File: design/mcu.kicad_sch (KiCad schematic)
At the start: 30 parts, among them J2 SWD_01X04, J3 DEBUG_SPI, U6 STM32H750VBTx, X1 ASTX-H11-25.000MHZ-T

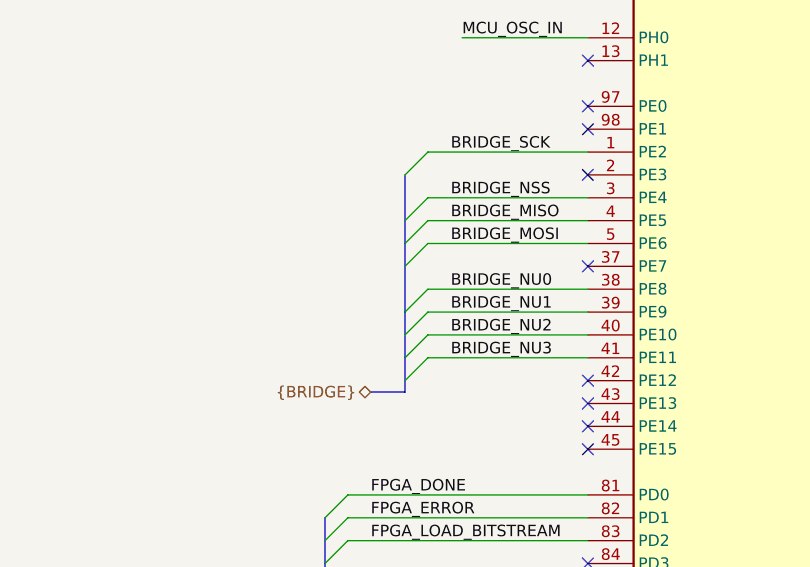
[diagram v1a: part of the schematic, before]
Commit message: Added RAM layout
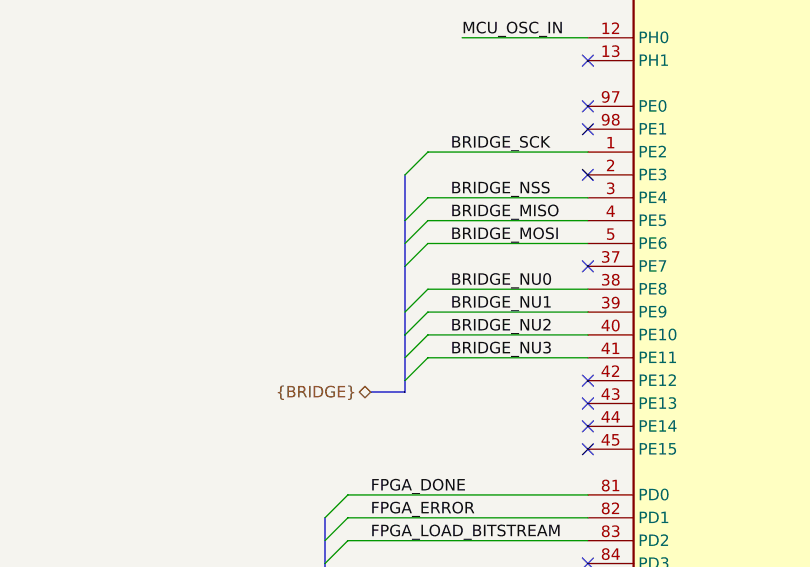
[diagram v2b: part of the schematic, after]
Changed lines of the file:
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@@
   (junction (at 236.22 25.4))
   (junction (at 262.89 26.67))
-  (no_connect (at 168.91 134.62))
-  (no_connect (at 168.91 86.36))
+  (no_connect (at 168.91 106.68))
+  (no_connect (at 168.91 127))
+  (no_connect (at 168.91 60.96))
+  (no_connect (at 168.91 129.54))
+  (no_connect (at 168.91 149.86))
   (no_connect (at 123.19 109.22))
   (no_connect (at 168.91 121.92))
+  (no_connect (at 168.91 53.34))
+  (no_connect (at 168.91 104.14))
+  (no_connect (at 123.19 144.78))
+  (no_connect (at 123.19 129.54))
+  (no_connect (at 168.91 116.84))
+  (no_connect (at 168.91 154.94))
+  (no_connect (at 168.91 119.38))
+  (no_connect (at 123.19 124.46))
+  (no_connect (at 168.91 50.8))
+  (no_connect (at 123.19 147.32))
+  (no_connect (at 168.91 86.36))
+  (no_connect (at 168.91 109.22))
+  (no_connect (at 123.19 162.56))
+  (no_connect (at 123.19 121.92))
+  (no_connect (at 168.91 170.18))
+  (no_connect (at 168.91 147.32))
+  (no_connect (at 168.91 167.64))
+  (no_connect (at 123.19 149.86))
+  (no_connect (at 123.19 142.24))
+  (no_connect (at 123.19 154.94))
+  (no_connect (at 168.91 142.24))
+  (no_connect (at 168.91 139.7))
+  (no_connect (at 168.91 134.62))
+  (no_connect (at 168.91 172.72))
+  (no_connect (at 168.91 165.1))
+  (no_connect (at 168.91 101.6))
+  (no_connect (at 123.19 91.44))
+  (no_connect (at 168.91 160.02))
+  (no_connect (at 168.91 68.58))
+  (no_connect (at 123.19 127))
+  (no_connect (at 168.91 162.56))
+  (no_connect (at 168.91 124.46))
+  (no_connect (at 168.91 63.5))
+  (no_connect (at 123.19 152.4))
+  (no_connect (at 168.91 114.3))
+  (no_connect (at 168.91 152.4))
   (no_connect (at 168.91 111.76))
-  (no_connect (at 168.91 172.72))
-  (no_connect (at 168.91 152.4))
+  (no_connect (at 123.19 86.36))
+  (no_connect (at 123.19 99.06))
+  (no_connect (at 168.91 137.16))
+  (no_connect (at 168.91 144.78))
+  (no_connect (at 123.19 93.98))
+  (no_connect (at 168.91 55.88))
   (no_connect (at 123.19 160.02))
-  (no_connect (at 168.91 154.94))
-  (no_connect (at 168.91 144.78))
-  (no_connect (at 123.19 142.24))
-  (no_connect (at 168.91 165.1))
-  (no_connect (at 168.91 119.38))
-  (no_connect (at 168.91 124.46))
-  (no_connect (at 123.19 91.44))
   (no_connect (at 168.91 66.04))
-  (no_connect (at 123.19 144.78))
-  (no_connect (at 168.91 167.64))
-  (no_connect (at 123.19 127))
   (no_connect (at 123.19 157.48))
-  (no_connect (at 168.91 127))
+  (no_connect (at 168.91 58.42))
   (no_connect (at 168.91 48.26))
-  (no_connect (at 123.19 152.4))
-  (no_connect (at 168.91 170.18))
-  (no_connect (at 123.19 162.56))
-  (no_connect (at 168.91 142.24))
-  (no_connect (at 168.91 63.5))
-  (no_connect (at 168.91 147.32))
-  (no_connect (at 123.19 99.06))
-  (no_connect (at 168.91 58.42))
-  (no_connect (at 123.19 124.46))
-  (no_connect (at 168.91 139.7))
-  (no_connect (at 168.91 50.8))
-  (no_connect (at 168.91 106.68))
-  (no_connect (at 123.19 86.36))
-  (no_connect (at 168.91 116.84))
-  (no_connect (at 168.91 109.22))
-  (no_connect (at 168.91 101.6))
-  (no_connect (at 168.91 60.96))
-  (no_connect (at 123.19 154.94))
-  (no_connect (at 123.19 129.54))
-  (no_connect (at 123.19 147.32))
-  (no_connect (at 123.19 93.98))
-  (no_connect (at 168.91 104.14))
-  (no_connect (at 168.91 149.86))
-  (no_connect (at 168.91 53.34))
-  (no_connect (at 168.91 114.3))
-  (no_connect (at 168.91 129.54))
-  (no_connect (at 168.91 55.88))
-  (no_connect (at 168.91 162.56))
-  (no_connect (at 168.91 137.16))
-  (no_connect (at 168.91 160.02))
-  (no_connect (at 123.19 121.92))
-  (no_connect (at 168.91 68.58))
-  (no_connect (at 123.19 149.86))
   (bus_entry (at 93.98 137.16) (size 2.54 -2.54))
   (bus_entry (at 93.98 139.7) (size 2.54 -2.54))
@@
   (bus (pts (xy 93.98 142.24) (xy 93.98 143.51)))
   (bus (pts (xy 99.06 123.19) (xy 102.87 123.19)))
-  (bus (pts (xy 102.87 99.06) (xy 102.87 106.68)))
-  (bus (pts (xy 102.87 106.68) (xy 102.87 114.3)))
-  (bus (pts (xy 102.87 114.3) (xy 102.87 119.38)))
-  (bus (pts (xy 102.87 119.38) (xy 102.87 123.19)))
+  (bus (pts (xy 102.87 99.06) (xy 102.87 104.14)))
+  (bus (pts (xy 102.87 104.14) (xy 102.87 109.22)))
+  (bus (pts (xy 102.87 109.22) (xy 102.87 116.84)))
+  (bus (pts (xy 102.87 116.84) (xy 102.87 121.92)))
+  (bus (pts (xy 102.87 121.92) (xy 102.87 123.19)))
   (bus (pts (xy 187.96 73.66) (xy 187.96 76.2)))
   (bus (pts (xy 187.96 76.2) (xy 187.96 81.28)))

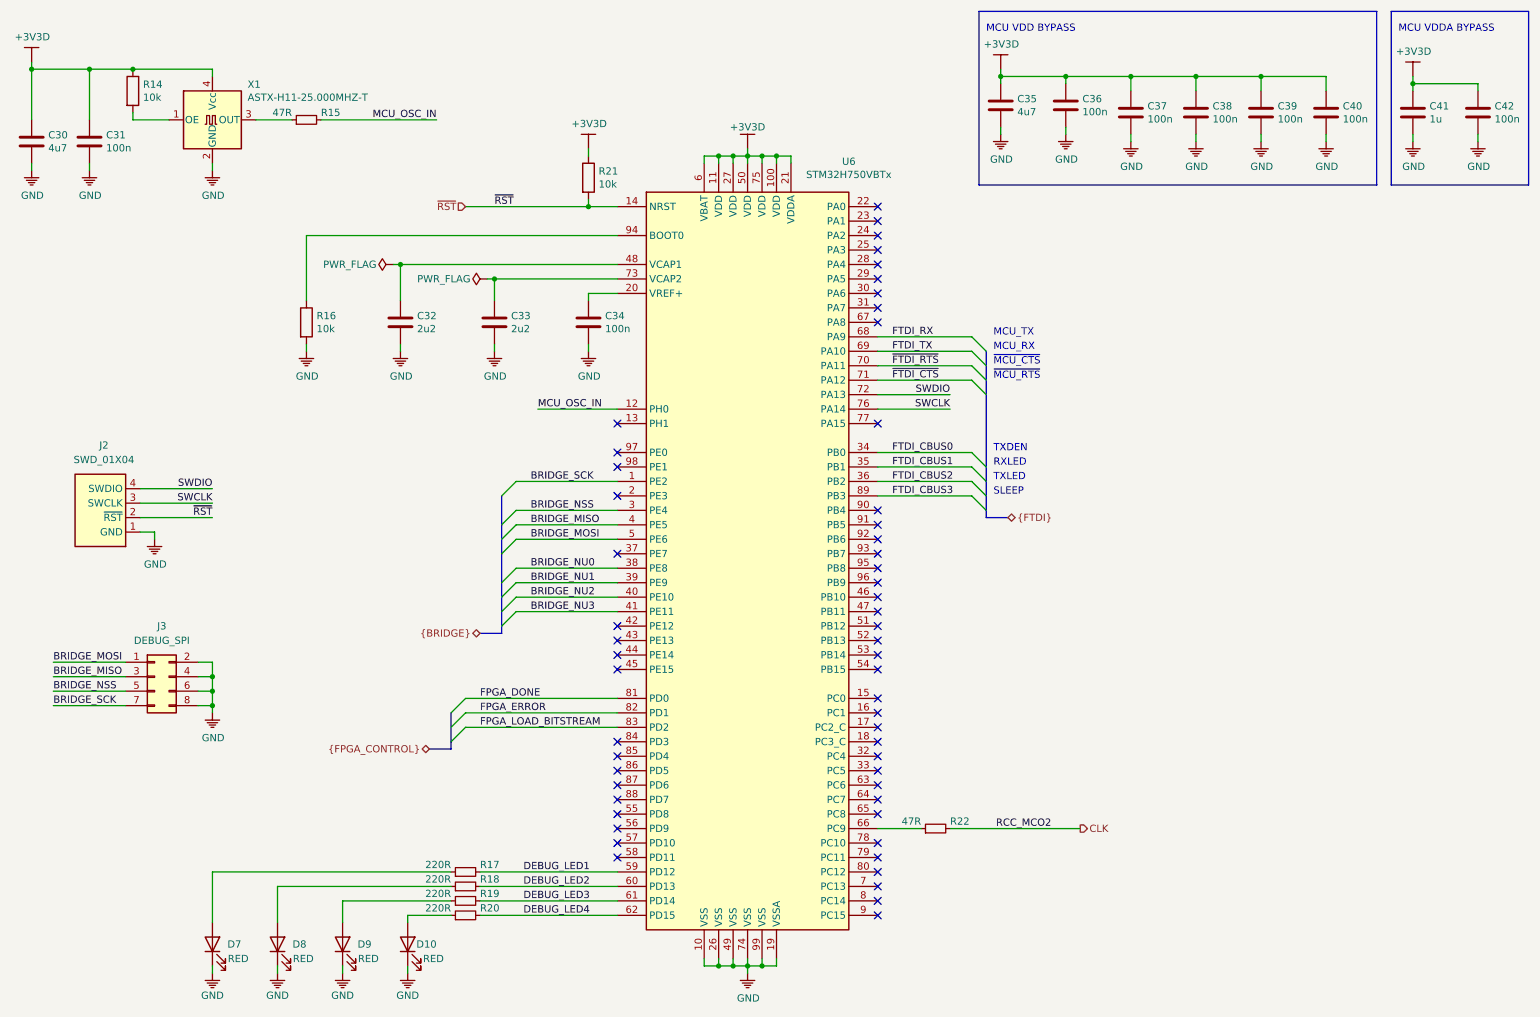
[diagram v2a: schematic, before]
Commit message: Updated layout
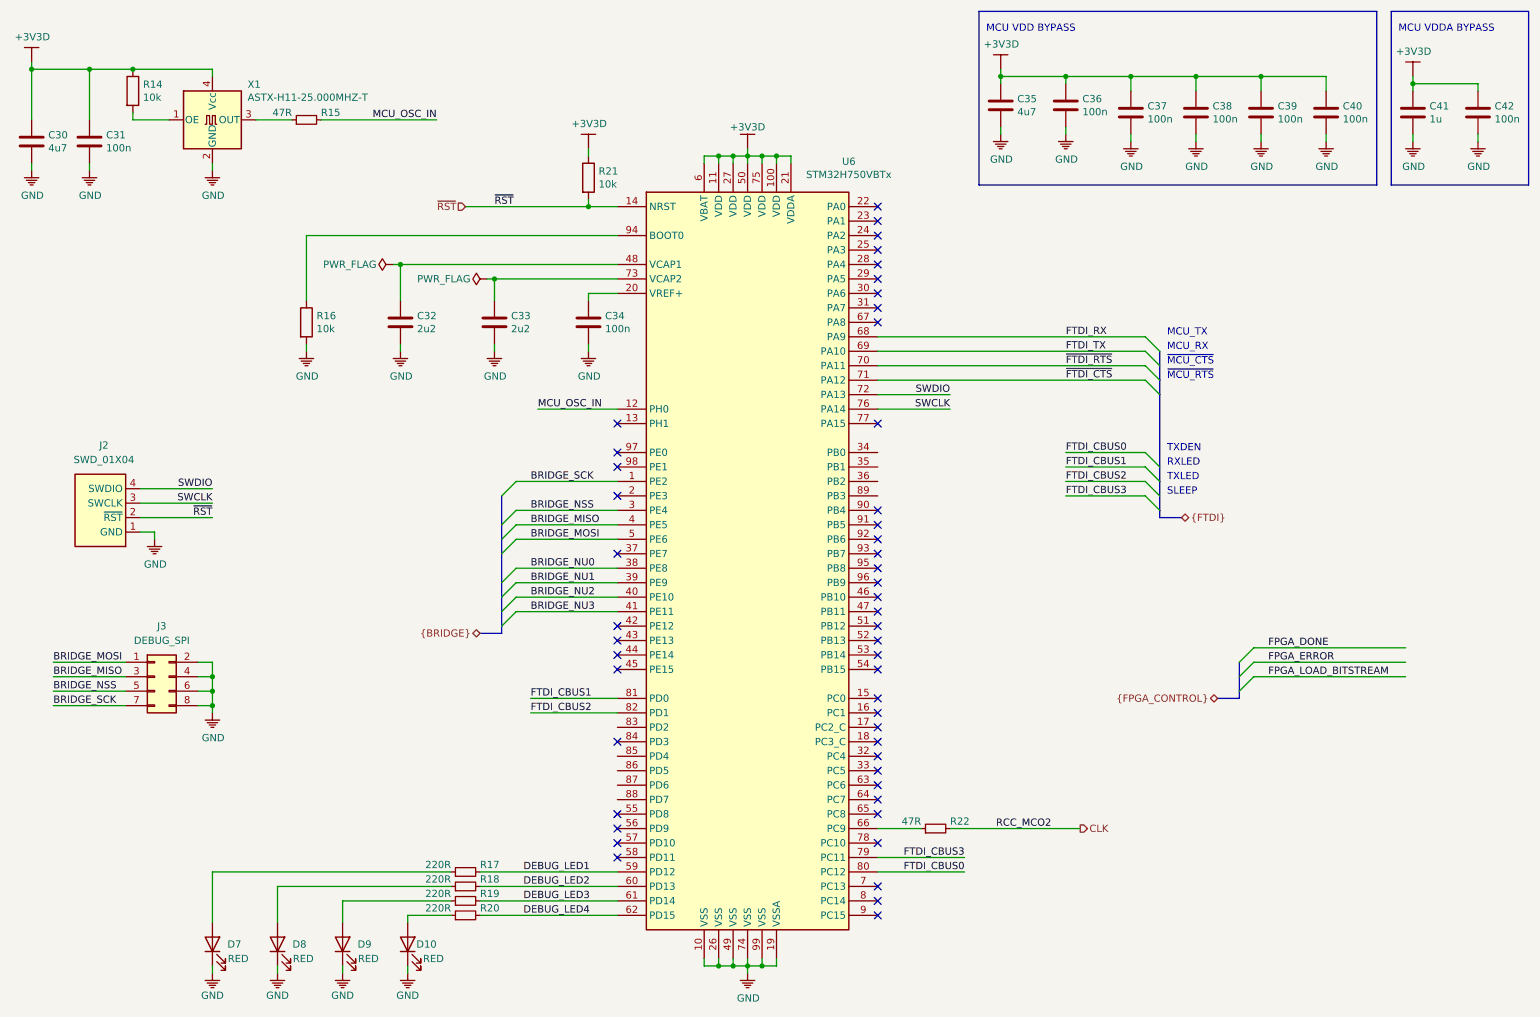
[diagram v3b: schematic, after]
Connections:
- net FPGA_DONE: no longer U6.81 (PD0)
- net FPGA_ERROR: no longer U6.82 (PD1)
- net FPGA_LOAD_BITSTREAM: no longer U6.83 (PD2)
- net FTDI_CBUS0: now also U6.80 (PC12); no longer U6.34 (PB0)
- net FTDI_CBUS1: now also U6.81 (PD0); no longer U6.35 (PB1)
- net FTDI_CBUS2: now also U6.82 (PD1); no longer U6.36 (PB2)
- net FTDI_CBUS3: now also U6.79 (PC11); no longer U6.89 (PB3)
- no-connect marks 55 -> 49

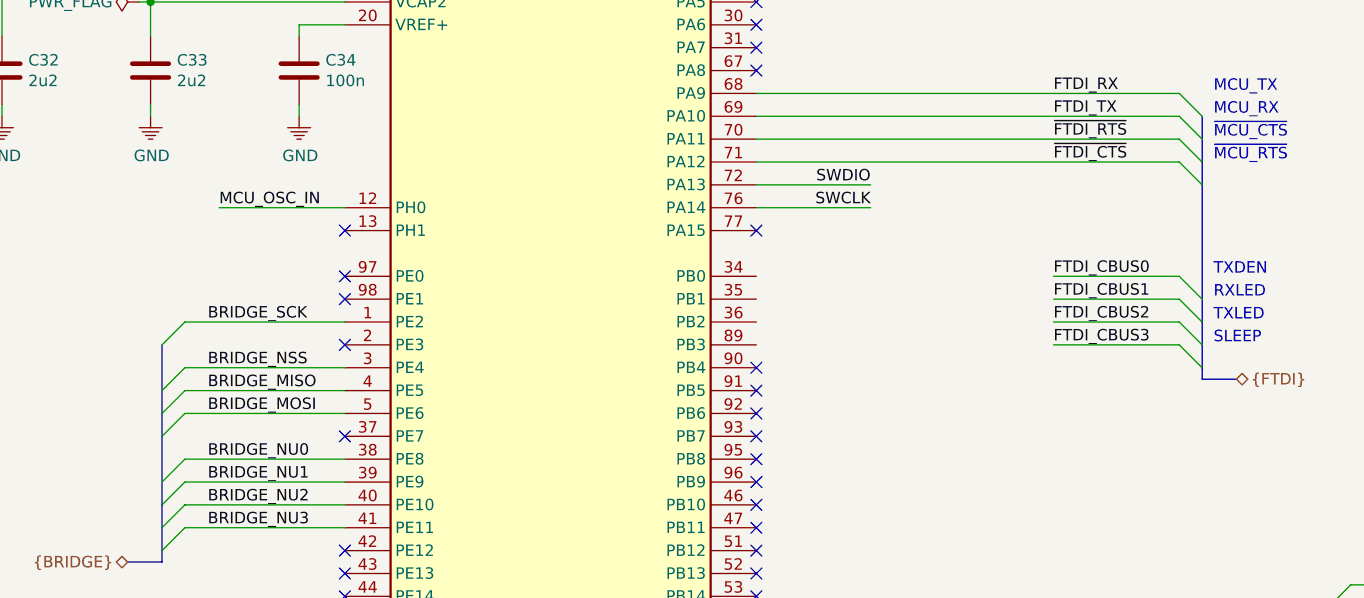
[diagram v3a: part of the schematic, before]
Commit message: Created new RAM placement and test layout
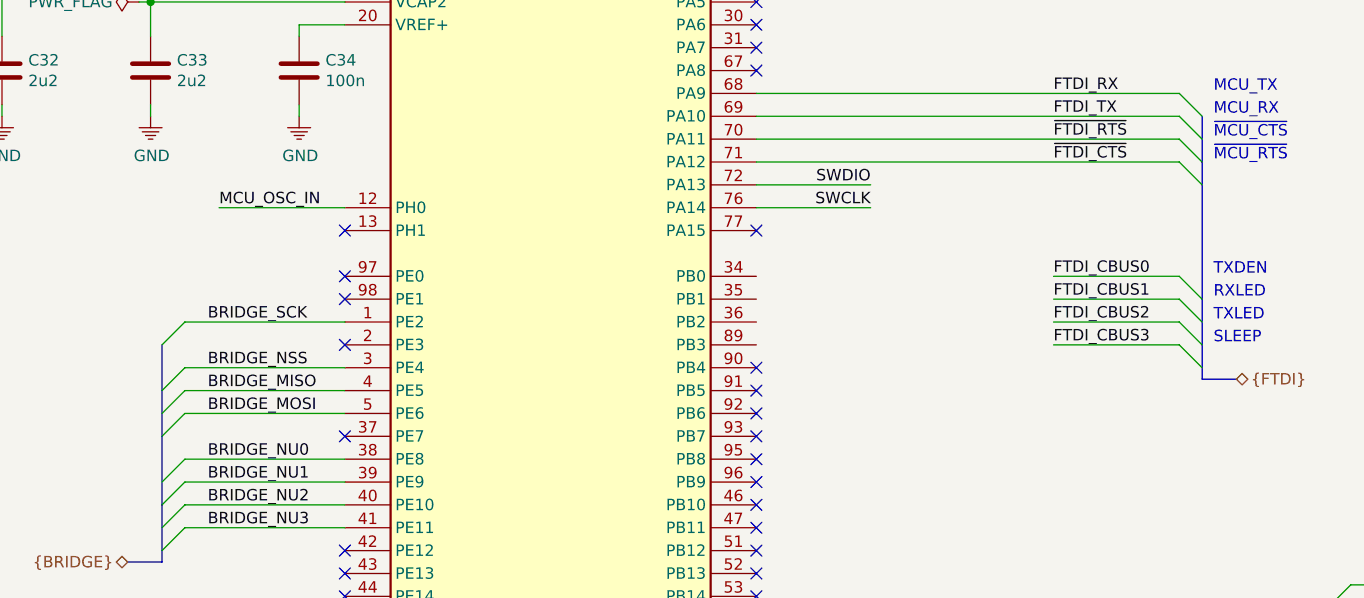
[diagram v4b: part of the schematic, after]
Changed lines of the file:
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@@
 (kicad_sch (version 20200512) (host eeschema "5.99.0-unknown-2cf82d9~101~ubuntu18.04.1")
-  (page 3 8)
+  (page 1 8)
   (paper "A4")
   (title_block
@@
   (junction (at 236.22 25.4))
   (junction (at 262.89 26.67))
+  (no_connect (at 123.19 124.46))
+  (no_connect (at 123.19 93.98))
+  (no_connect (at 168.91 116.84))
+  (no_connect (at 168.91 144.78))
+  (no_connect (at 123.19 157.48))
+  (no_connect (at 168.91 101.6))
+  (no_connect (at 168.91 160.02))
+  (no_connect (at 168.91 48.26))
+  (no_connect (at 168.91 129.54))
+  (no_connect (at 168.91 170.18))
+  (no_connect (at 123.19 142.24))
+  (no_connect (at 168.91 154.94))
+  (no_connect (at 168.91 134.62))
+  (no_connect (at 168.91 58.42))
+  (no_connect (at 123.19 121.92))
+  (no_connect (at 168.91 167.64))
+  (no_connect (at 168.91 124.46))
+  (no_connect (at 123.19 99.06))
+  (no_connect (at 168.91 104.14))
+  (no_connect (at 168.91 55.88))
+  (no_connect (at 168.91 60.96))
+  (no_connect (at 123.19 160.02))
+  (no_connect (at 168.91 172.72))
+  (no_connect (at 123.19 162.56))
+  (no_connect (at 123.19 86.36))
+  (no_connect (at 168.91 121.92))
+  (no_connect (at 168.91 68.58))
   (no_connect (at 168.91 114.3))
-  (no_connect (at 168.91 121.92))
-  (no_connect (at 168.91 104.14))
+  (no_connect (at 168.91 86.36))
+  (no_connect (at 123.19 127))
+  (no_connect (at 168.91 66.04))
+  (no_connect (at 168.91 106.68))
+  (no_connect (at 168.91 139.7))
+  (no_connect (at 168.91 152.4))
+  (no_connect (at 168.91 149.86))
   (no_connect (at 123.19 91.44))
-  (no_connect (at 168.91 106.68))
-  (no_connect (at 123.19 93.98))
-  (no_connect (at 123.19 127))
+  (no_connect (at 168.91 137.16))
+  (no_connect (at 168.91 119.38))
+  (no_connect (at 168.91 63.5))
+  (no_connect (at 168.91 109.22))
+  (no_connect (at 168.91 53.34))
   (no_connect (at 168.91 142.24))
-  (no_connect (at 168.91 154.94))
-  (no_connect (at 168.91 66.04))
-  (no_connect (at 123.19 124.46))
-  (no_connect (at 168.91 60.96))
+  (no_connect (at 123.19 154.94))
+  (no_connect (at 123.19 129.54))
+  (no_connect (at 168.91 147.32))
+  (no_connect (at 123.19 109.22))
   (no_connect (at 168.91 127))
-  (no_connect (at 168.91 109.22))
-  (no_connect (at 168.91 172.72))
-  (no_connect (at 168.91 134.62))
-  (no_connect (at 123.19 129.54))
-  (no_connect (at 168.91 63.5))
-  (no_connect (at 168.91 167.64))
-  (no_connect (at 123.19 99.06))
-  (no_connect (at 168.91 152.4))
-  (no_connect (at 123.19 109.22))
-  (no_connect (at 168.91 149.86))
-  (no_connect (at 168.91 86.36))
-  (no_connect (at 168.91 129.54))
   (no_connect (at 168.91 50.8))
-  (no_connect (at 168.91 124.46))
-  (no_connect (at 168.91 160.02))
-  (no_connect (at 168.91 101.6))
-  (no_connect (at 168.91 58.42))
   (no_connect (at 168.91 111.76))
-  (no_connect (at 168.91 119.38))
-  (no_connect (at 168.91 139.7))
-  (no_connect (at 168.91 137.16))
-  (no_connect (at 123.19 142.24))
-  (no_connect (at 168.91 55.88))
-  (no_connect (at 168.91 144.78))
-  (no_connect (at 123.19 154.94))
-  (no_connect (at 168.91 116.84))
-  (no_connect (at 123.19 157.48))
-  (no_connect (at 123.19 121.92))
-  (no_connect (at 123.19 160.02))
-  (no_connect (at 168.91 48.26))
-  (no_connect (at 168.91 147.32))
-  (no_connect (at 123.19 86.36))
-  (no_connect (at 168.91 170.18))
-  (no_connect (at 168.91 68.58))
-  (no_connect (at 168.91 53.34))
-  (no_connect (at 123.19 162.56))
   (bus_entry (at 102.87 99.06) (size 2.54 -2.54))
   (bus_entry (at 102.87 104.14) (size 2.54 -2.54))
@@
   (wire (pts (xy 274.32 35.56) (xy 274.32 36.83)))
   (bus (pts (xy 99.06 123.19) (xy 102.87 123.19)))
-  (bus (pts (xy 102.87 99.06) (xy 102.87 106.68)))
-  (bus (pts (xy 102.87 106.68) (xy 102.87 109.22)))
+  (bus (pts (xy 102.87 99.06) (xy 102.87 104.14)))
+  (bus (pts (xy 102.87 104.14) (xy 102.87 109.22)))
   (bus (pts (xy 102.87 109.22) (xy 102.87 116.84)))
   (bus (pts (xy 102.87 116.84) (xy 102.87 121.92)))
   (bus (pts (xy 102.87 121.92) (xy 102.87 123.19)))
   (bus (pts (xy 218.44 73.66) (xy 218.44 78.74)))
-  (bus (pts (xy 218.44 78.74) (xy 218.44 81.28)))
-  (bus (pts (xy 218.44 81.28) (xy 218.44 96.52)))
-  (bus (pts (xy 218.44 96.52) (xy 218.44 101.6)))
-  (bus (pts (xy 218.44 101.6) (xy 218.44 102.87)))
+  (bus (pts (xy 218.44 78.74) (xy 218.44 93.98)))
+  (bus (pts (xy 218.44 93.98) (xy 218.44 99.06)))
+  (bus (pts (xy 218.44 99.06) (xy 218.44 102.87)))
   (bus (pts (xy 218.44 102.87) (xy 222.25 102.87)))
   (bus (pts (xy 228.6 134.62) (xy 232.41 134.62)))
